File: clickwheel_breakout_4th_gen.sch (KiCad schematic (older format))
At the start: 7 parts, among them J1 SFV8R-2STE1HLF, J2 SFV14R-2STE1HLF, J3 SFV8R-2STE1HLF, J4 SFV14R-2STE1HLF, J5 Conn_02x08_Odd_Even, J6 Conn_02x14_Odd_Even, J7 USB_C_Receptacle_USB2.0

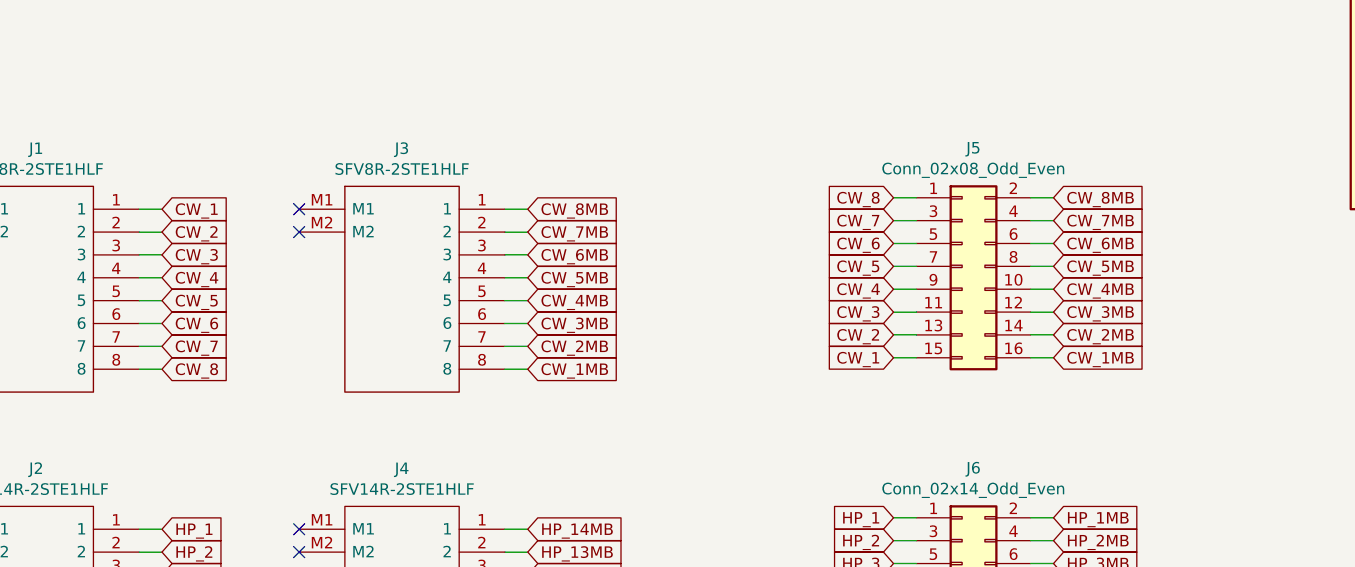
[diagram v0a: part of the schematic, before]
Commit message: Add known clickwheel signal names
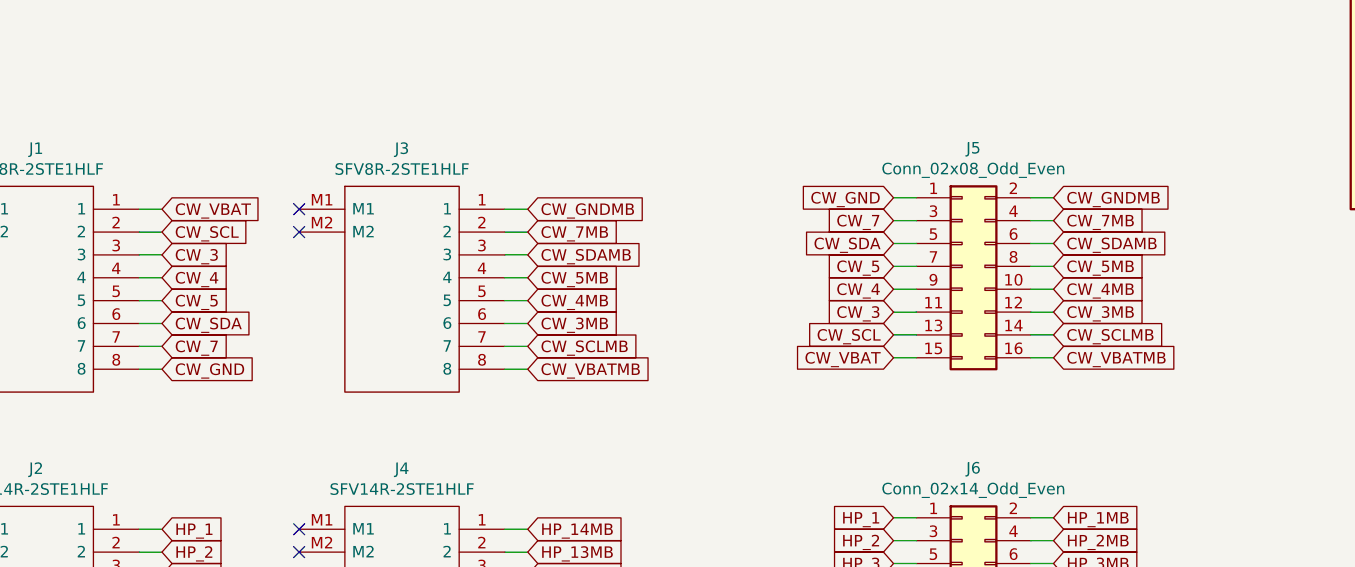
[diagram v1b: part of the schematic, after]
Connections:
- net CW_1 renamed CW_VBAT
- net CW_1MB renamed CW_VBATMB
- net CW_2 renamed CW_SCL
- net CW_2MB renamed CW_SCLMB
- net CW_6 renamed CW_SDA
- net CW_6MB renamed CW_SDAMB
- net CW_8 renamed CW_GND
- net CW_8MB renamed CW_GNDMB
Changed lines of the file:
@@
 NoConn ~ 1500 3150
 Text GLabel 2500 3050 2    50   Input ~ 0
-CW_1
+CW_VBAT
 Wire Wire Line
 	2400 3050 2500 3050
 Text GLabel 2500 3150 2    50   Input ~ 0
-CW_2
+CW_SCL
 Wire Wire Line
 	2400 3150 2500 3150
@@
 	2400 3450 2500 3450
 Text GLabel 2500 3550 2    50   Input ~ 0
-CW_6
+CW_SDA
 Wire Wire Line
 	2400 3550 2500 3550
@@
 	2400 3650 2500 3650
 Text GLabel 2500 3750 2    50   Input ~ 0
-CW_8
+CW_GND
 Wire Wire Line
 	2400 3750 2500 3750
@@
 NoConn ~ 3100 4550
 Text GLabel 4100 3750 2    50   Input ~ 0
-CW_1MB
+CW_VBATMB
 Wire Wire Line
 	4000 3750 4100 3750
 Text GLabel 4100 3650 2    50   Input ~ 0
-CW_2MB
+CW_SCLMB
 Wire Wire Line
 	4000 3650 4100 3650
@@
 	4000 3350 4100 3350
 Text GLabel 4100 3250 2    50   Input ~ 0
-CW_6MB
+CW_SDAMB
 Wire Wire Line
 	4000 3250 4100 3250
@@
 	4000 3150 4100 3150
 Text GLabel 4100 3050 2    50   Input ~ 0
-CW_8MB
+CW_GNDMB
 Wire Wire Line
 	4000 3050 4100 3050
@@
 	4000 4450 4100 4450
 Text GLabel 6400 3700 2    50   Input ~ 0
-CW_1MB
+CW_VBATMB
 Wire Wire Line
 	6300 3700 6400 3700
 Text GLabel 6400 3600 2    50   Input ~ 0
-CW_2MB
+CW_SCLMB
 Wire Wire Line
 	6300 3600 6400 3600
@@
 	6300 3300 6400 3300
 Text GLabel 6400 3200 2    50   Input ~ 0
-CW_6MB
+CW_SDAMB
 Wire Wire Line
 	6300 3200 6400 3200
@@
 	6300 3100 6400 3100
 Text GLabel 6400 3000 2    50   Input ~ 0
-CW_8MB
+CW_GNDMB
 Wire Wire Line
 	6300 3000 6400 3000
@@
 	5800 3000 5700 3000
 Text GLabel 5700 3000 0    50   Input ~ 0
-CW_8
+CW_GND
 Wire Wire Line
 	5800 3100 5700 3100
@@
 	5800 3200 5700 3200
 Text GLabel 5700 3200 0    50   Input ~ 0
-CW_6
+CW_SDA
 Wire Wire Line
 	5800 3300 5700 3300
@@
 	5800 3600 5700 3600
 Text GLabel 5700 3600 0    50   Input ~ 0
-CW_2
+CW_SCL
 Wire Wire Line
 	5800 3700 5700 3700
 Text GLabel 5700 3700 0    50   Input ~ 0
-CW_1
+CW_VBAT
 $Comp
 L Connector:USB_C_Receptacle_USB2.0 J7

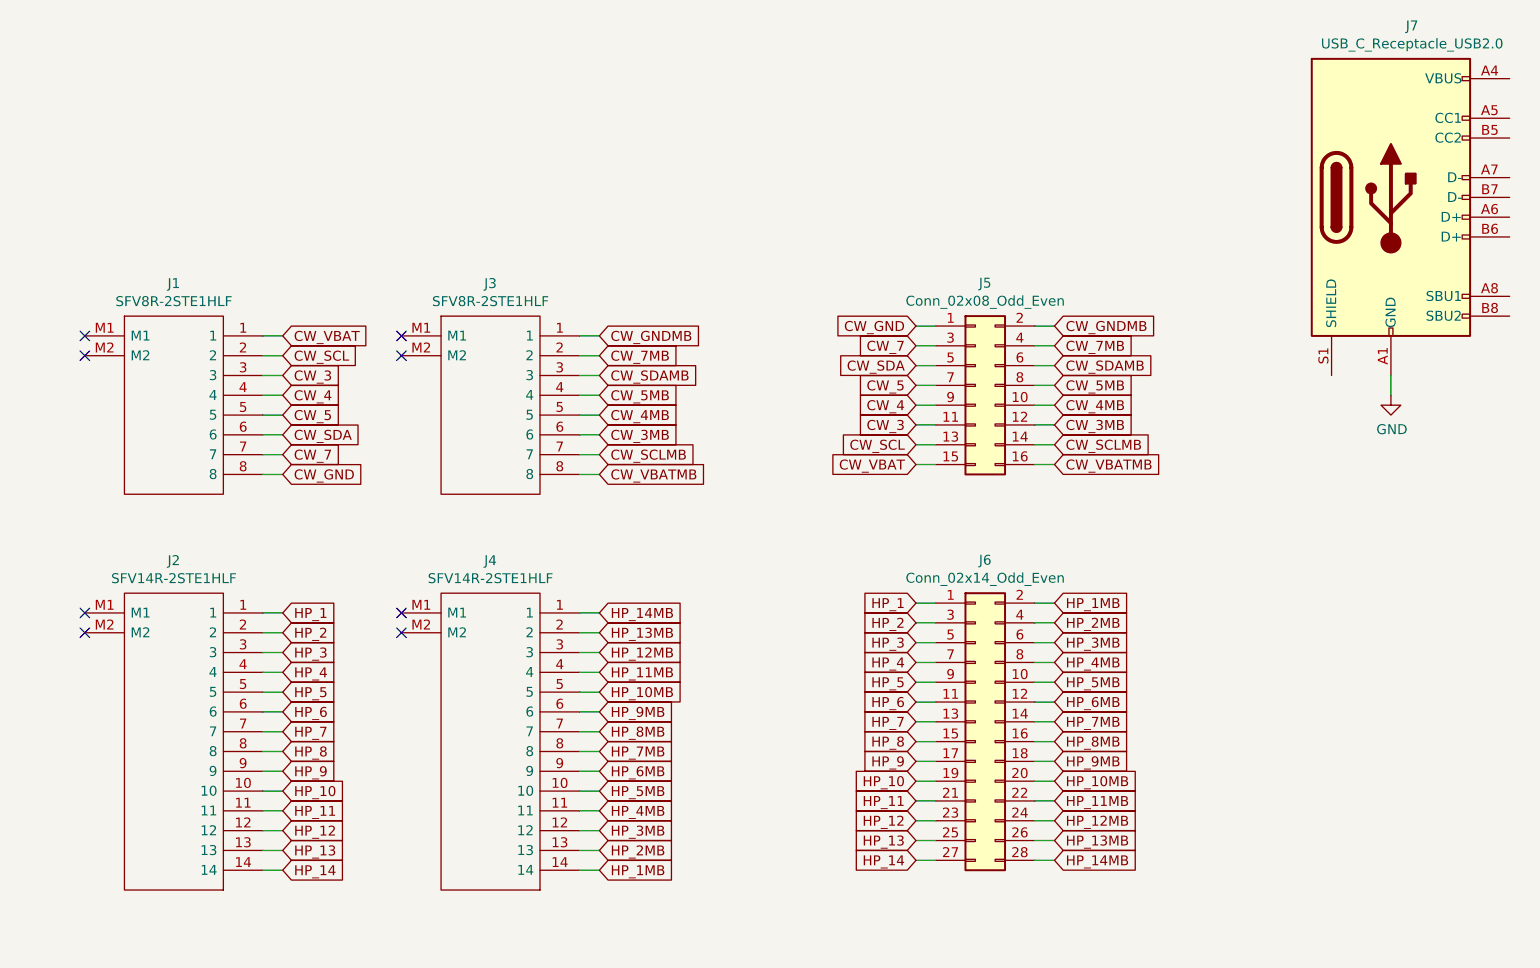
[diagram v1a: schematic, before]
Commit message: Add known headphone signal names with silkscreen
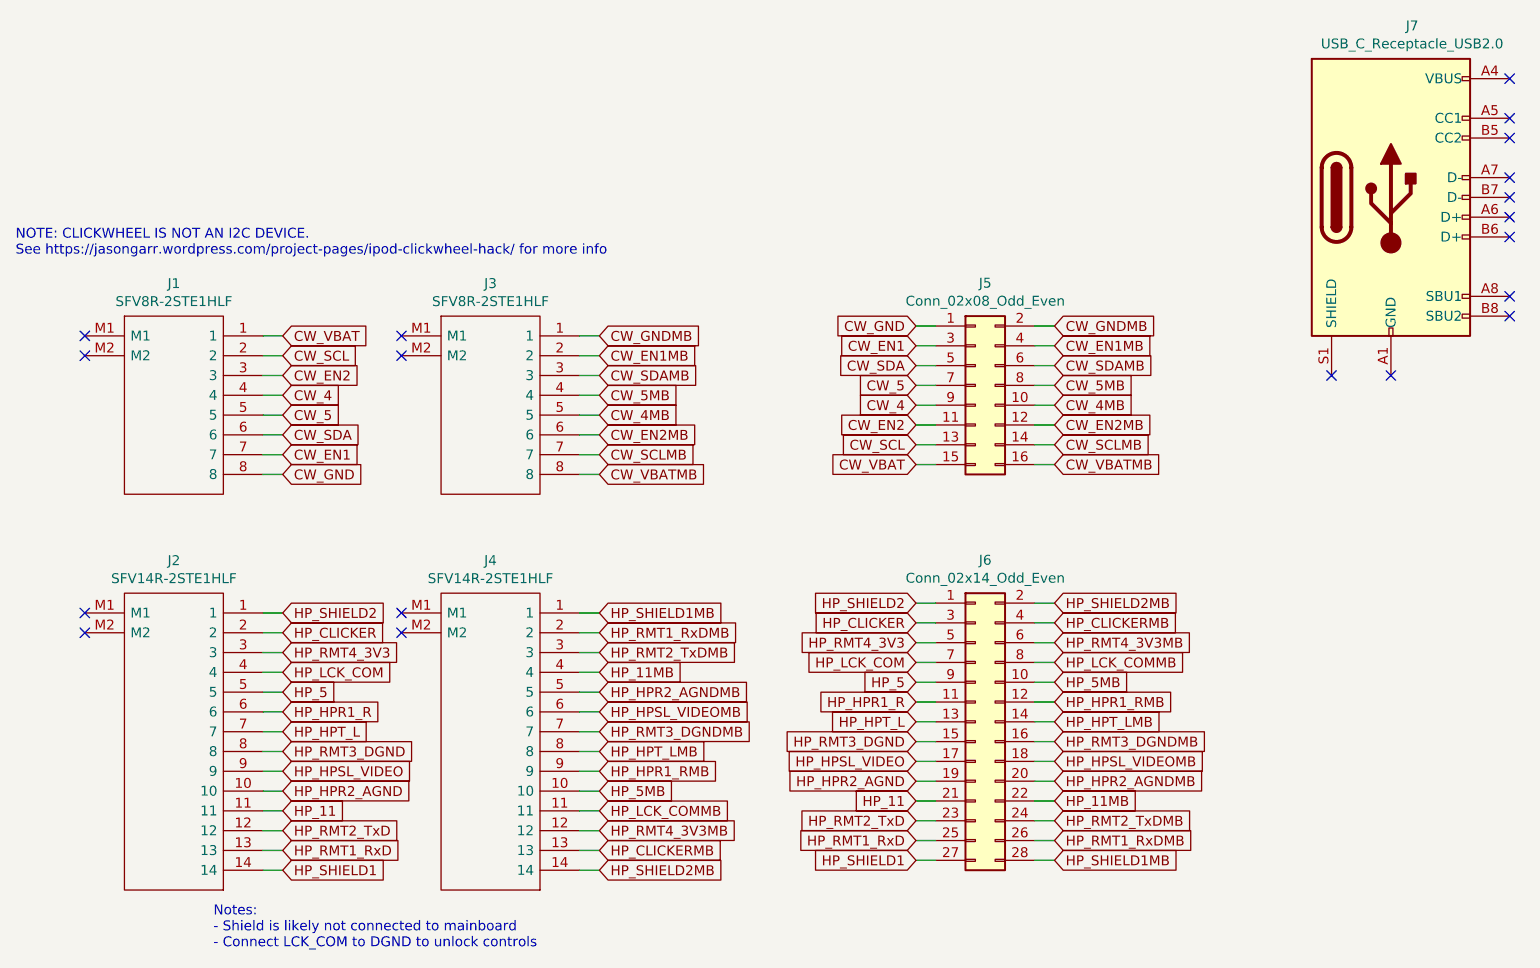
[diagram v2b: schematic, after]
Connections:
- net CW_3 renamed CW_EN2
- net CW_3MB renamed CW_EN2MB
- net CW_7 renamed CW_EN1
- net CW_7MB renamed CW_EN1MB
- net GND: no longer names the net of J7.A1 (GND), J7.A12 (GND), J7.B1 (GND), J7.B12 (GND)
- net HP_1 renamed HP_SHIELD2
- net HP_10 renamed HP_HPR2_AGND
- net HP_10MB renamed HP_HPR2_AGNDMB
- net HP_12 renamed HP_RMT2_TxD
- net HP_12MB renamed HP_RMT2_TxDMB
- net HP_13 renamed HP_RMT1_RxD
- net HP_13MB renamed HP_RMT1_RxDMB
- net HP_14 renamed HP_SHIELD1
- net HP_14MB renamed HP_SHIELD1MB
- net HP_1MB renamed HP_SHIELD2MB
- net HP_2 renamed HP_CLICKER
- net HP_2MB renamed HP_CLICKERMB
- net HP_3 renamed HP_RMT4_3V3
- net HP_3MB renamed HP_RMT4_3V3MB
- net HP_4 renamed HP_LCK_COM
- net HP_4MB renamed HP_LCK_COMMB
- net HP_6 renamed HP_HPR1_R
- net HP_6MB renamed HP_HPR1_RMB
- net HP_7 renamed HP_HPT_L
- net HP_7MB renamed HP_HPT_LMB
- net HP_8 renamed HP_RMT3_DGND
- net HP_8MB renamed HP_RMT3_DGNDMB
- net HP_9 renamed HP_HPSL_VIDEO
- net HP_9MB renamed HP_HPSL_VIDEOMB
- no-connect marks 8 -> 19
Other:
- note added: "NOTE: CLICKWHEEL IS NOT AN I2C DEVICE.\nSee https://jasongarr.wordpress.com/project-pages/ipod-clickwheel-hack/ for more info"
- note added: "Notes: \n- Shield is likely not connected to mainboard\n- Connect LCK_COM to DGND to unlock controls"
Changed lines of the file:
@@
 	2400 3150 2500 3150
 Text GLabel 2500 3250 2    50   Input ~ 0
-CW_3
+CW_EN2
 Wire Wire Line
 	2400 3250 2500 3250
@@
 	2400 3550 2500 3550
 Text GLabel 2500 3650 2    50   Input ~ 0
-CW_7
+CW_EN1
 Wire Wire Line
 	2400 3650 2500 3650
@@
 	2400 3750 2500 3750
 Text GLabel 2500 4450 2    50   Input ~ 0
-HP_1
+HP_SHIELD2
 Wire Wire Line
 	2400 4450 2500 4450
@@
 NoConn ~ 1500 4550
 Text GLabel 2500 4550 2    50   Input ~ 0
-HP_2
+HP_CLICKER
 Wire Wire Line
 	2400 4550 2500 4550
 Text GLabel 2500 4650 2    50   Input ~ 0
-HP_3
+HP_RMT4_3V3
 Wire Wire Line
 	2400 4650 2500 4650
 Text GLabel 2500 4750 2    50   Input ~ 0
-HP_4
+HP_LCK_COM
 Wire Wire Line
 	2400 4750 2500 4750
@@
 	2400 4850 2500 4850
 Text GLabel 2500 4950 2    50   Input ~ 0
-HP_6
+HP_HPR1_R
 Wire Wire Line
 	2400 4950 2500 4950
 Text GLabel 2500 5050 2    50   Input ~ 0
-HP_7
+HP_HPT_L
 Wire Wire Line
 	2400 5050 2500 5050
 Text GLabel 2500 5150 2    50   Input ~ 0
-HP_8
+HP_RMT3_DGND
 Wire Wire Line
 	2400 5150 2500 5150
 Text GLabel 2500 5250 2    50   Input ~ 0
-HP_9
+HP_HPSL_VIDEO
 Wire Wire Line
 	2400 5250 2500 5250
 Text GLabel 2500 5350 2    50   Input ~ 0
-HP_10
+HP_HPR2_AGND
 Wire Wire Line
 	2400 5350 2500 5350
@@
 	2400 5450 2500 5450
 Text GLabel 2500 5550 2    50   Input ~ 0
-HP_12
+HP_RMT2_TxD
 Wire Wire Line
 	2400 5550 2500 5550
 Text GLabel 2500 5650 2    50   Input ~ 0
-HP_13
+HP_RMT1_RxD
 Wire Wire Line
 	2400 5650 2500 5650
 Text GLabel 2500 5750 2    50   Input ~ 0
-HP_14
+HP_SHIELD1
 Wire Wire Line
 	2400 5750 2500 5750
@@
 	4000 3650 4100 3650
 Text GLabel 4100 3550 2    50   Input ~ 0
-CW_3MB
+CW_EN2MB
 Wire Wire Line
 	4000 3550 4100 3550
@@
 	4000 3250 4100 3250
 Text GLabel 4100 3150 2    50   Input ~ 0
-CW_7MB
+CW_EN1MB
 Wire Wire Line
 	4000 3150 4100 3150
@@
 	4000 3050 4100 3050
 Text GLabel 4100 5750 2    50   Input ~ 0
-HP_1MB
+HP_SHIELD2MB
 Wire Wire Line
 	4000 5750 4100 5750
 Text GLabel 4100 5650 2    50   Input ~ 0
-HP_2MB
+HP_CLICKERMB
 Wire Wire Line
 	4000 5650 4100 5650
 Text GLabel 4100 5550 2    50   Input ~ 0
-HP_3MB
+HP_RMT4_3V3MB
 Wire Wire Line
 	4000 5550 4100 5550
 Text GLabel 4100 5450 2    50   Input ~ 0
-HP_4MB
+HP_LCK_COMMB
 Wire Wire Line
 	4000 5450 4100 5450
@@
 	4000 5350 4100 5350
 Text GLabel 4100 5250 2    50   Input ~ 0
-HP_6MB
+HP_HPR1_RMB
 Wire Wire Line
 	4000 5250 4100 5250
 Text GLabel 4100 5150 2    50   Input ~ 0
-HP_7MB
+HP_HPT_LMB
 Wire Wire Line
 	4000 5150 4100 5150
 Text GLabel 4100 5050 2    50   Input ~ 0
-HP_8MB
+HP_RMT3_DGNDMB
 Wire Wire Line
 	4000 5050 4100 5050
 Text GLabel 4100 4950 2    50   Input ~ 0
-HP_9MB
+HP_HPSL_VIDEOMB
 Wire Wire Line
 	4000 4950 4100 4950
 Text GLabel 4100 4850 2    50   Input ~ 0
-HP_10MB
+HP_HPR2_AGNDMB
 Wire Wire Line
 	4000 4850 4100 4850
@@
 	4000 4750 4100 4750
 Text GLabel 4100 4650 2    50   Input ~ 0
-HP_12MB
+HP_RMT2_TxDMB
 Wire Wire Line
 	4000 4650 4100 4650
 Text GLabel 4100 4550 2    50   Input ~ 0
-HP_13MB
+HP_RMT1_RxDMB
 Wire Wire Line
 	4000 4550 4100 4550
 Text GLabel 4100 4450 2    50   Input ~ 0
-HP_14MB
+HP_SHIELD1MB
 Wire Wire Line
 	4000 4450 4100 4450
@@
 	6300 3600 6400 3600
 Text GLabel 6400 3500 2    50   Input ~ 0
-CW_3MB
+CW_EN2MB
 Wire Wire Line
 	6300 3500 6400 3500
@@
 	6300 3200 6400 3200
 Text GLabel 6400 3100 2    50   Input ~ 0
-CW_7MB
+CW_EN1MB
 Wire Wire Line
 	6300 3100 6400 3100
@@
 $EndComp
 Text GLabel 6400 4400 2    50   Input ~ 0
-HP_1MB
+HP_SHIELD2MB
 Wire Wire Line
 	6300 4400 6400 4400
 Text GLabel 6400 4500 2    50   Input ~ 0
-HP_2MB
+HP_CLICKERMB
 Wire Wire Line
 	6300 4500 6400 4500
 Text GLabel 6400 4600 2    50   Input ~ 0
-HP_3MB
+HP_RMT4_3V3MB
 Wire Wire Line
 	6300 4600 6400 4600
 Text GLabel 6400 4700 2    50   Input ~ 0
-HP_4MB
+HP_LCK_COMMB
 Wire Wire Line
 	6300 4700 6400 4700
@@
 	6300 4800 6400 4800
 Text GLabel 6400 4900 2    50   Input ~ 0
-HP_6MB
+HP_HPR1_RMB
 Wire Wire Line
 	6300 4900 6400 4900
 Text GLabel 6400 5000 2    50   Input ~ 0
-HP_7MB
+HP_HPT_LMB
 Wire Wire Line
 	6300 5000 6400 5000
 Text GLabel 6400 5100 2    50   Input ~ 0
-HP_8MB
+HP_RMT3_DGNDMB
 Wire Wire Line
 	6300 5100 6400 5100
 Text GLabel 6400 5200 2    50   Input ~ 0
-HP_9MB
+HP_HPSL_VIDEOMB
 Wire Wire Line
 	6300 5200 6400 5200
 Text GLabel 6400 5300 2    50   Input ~ 0
-HP_10MB
+HP_HPR2_AGNDMB
 Wire Wire Line
 	6300 5300 6400 5300
@@
 	6300 5400 6400 5400
 Text GLabel 6400 5500 2    50   Input ~ 0
-HP_12MB
+HP_RMT2_TxDMB
 Wire Wire Line
 	6300 5500 6400 5500
 Text GLabel 6400 5600 2    50   Input ~ 0
-HP_13MB
+HP_RMT1_RxDMB
 Wire Wire Line
 	6300 5600 6400 5600
 Text GLabel 6400 5700 2    50   Input ~ 0
-HP_14MB
+HP_SHIELD1MB
 Wire Wire Line
 	6300 5700 6400 5700
 Text GLabel 5700 4400 0    50   Input ~ 0
-HP_1
+HP_SHIELD2
 Wire Wire Line
 	5800 4400 5700 4400
 Text GLabel 5700 4500 0    50   Input ~ 0
-HP_2
+HP_CLICKER
 Wire Wire Line
 	5800 4500 5700 4500
 Text GLabel 5700 4600 0    50   Input ~ 0
-HP_3
+HP_RMT4_3V3
 Wire Wire Line
 	5800 4600 5700 4600
 Text GLabel 5700 4700 0    50   Input ~ 0
-HP_4
+HP_LCK_COM
 Wire Wire Line
 	5800 4700 5700 4700
@@
 	5800 4800 5700 4800
 Text GLabel 5700 4900 0    50   Input ~ 0
-HP_6
+HP_HPR1_R
 Wire Wire Line
 	5800 4900 5700 4900
 Text GLabel 5700 5000 0    50   Input ~ 0
-HP_7
+HP_HPT_L
 Wire Wire Line
 	5800 5000 5700 5000
 Text GLabel 5700 5100 0    50   Input ~ 0
-HP_8
+HP_RMT3_DGND
 Wire Wire Line
 	5800 5100 5700 5100
 Text GLabel 5700 5200 0    50   Input ~ 0
-HP_9
+HP_HPSL_VIDEO
 Wire Wire Line
 	5800 5200 5700 5200
 Text GLabel 5700 5300 0    50   Input ~ 0
-HP_10
+HP_HPR2_AGND
 Wire Wire Line
 	5800 5300 5700 5300
@@
 	5800 5400 5700 5400
 Text GLabel 5700 5500 0    50   Input ~ 0
-HP_12
+HP_RMT2_TxD
 Wire Wire Line
 	5800 5500 5700 5500
 Text GLabel 5700 5600 0    50   Input ~ 0
-HP_13
+HP_RMT1_RxD
 Wire Wire Line
 	5800 5600 5700 5600
 Text GLabel 5700 5700 0    50   Input ~ 0
-HP_14
+HP_SHIELD1
 Wire Wire Line
 	5800 5700 5700 5700
@@
 	5800 3100 5700 3100
 Text GLabel 5700 3100 0    50   Input ~ 0
-CW_7
+CW_EN1
 Wire Wire Line
 	5800 3200 5700 3200
@@
 	5800 3500 5700 3500
 Text GLabel 5700 3500 0    50   Input ~ 0
-CW_3
+CW_EN2
 Wire Wire Line
 	5800 3600 5700 3600
@@
 	1    0    0    -1
 $EndComp
-$Comp
-L power:GND #PWR0101
-U 1 1 5F693C0F
-P 8100 3350
-F 0 "#PWR0101" H 8100 3100 50  0001 C CNN
-F 1 "GND" H 8105 3177 50  0000 C CNN
-F 2 "" H 8100 3350 50  0001 C CNN
-F 3 "" H 8100 3350 50  0001 C CNN
-	1    8100 3350
-	1    0    0    -1
-$EndComp
-Wire Wire Line
-	8100 3350 8100 3250
+Text Notes 1150 2650 0    50   ~ 0
+NOTE: CLICKWHEEL IS NOT AN I2C DEVICE.\nSee https://jasongarr.wordpress.com/project-pages/ipod-clickwheel-hack/ for more info
+NoConn ~ 7800 3250
+Text Notes 2150 6150 0    50   ~ 0
+Notes: \n- Shield is likely not connected to mainboard\n- Connect LCK_COM to DGND to unlock controls
+NoConn ~ 8100 3250
+NoConn ~ 8700 2950
+NoConn ~ 8700 2850
+NoConn ~ 8700 2550
+NoConn ~ 8700 2450
+NoConn ~ 8700 2350
+NoConn ~ 8700 2250
+NoConn ~ 8700 2050
+NoConn ~ 8700 1950
+NoConn ~ 8700 1750
 $EndSCHEMATC
